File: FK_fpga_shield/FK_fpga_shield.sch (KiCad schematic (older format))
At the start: 3 parts

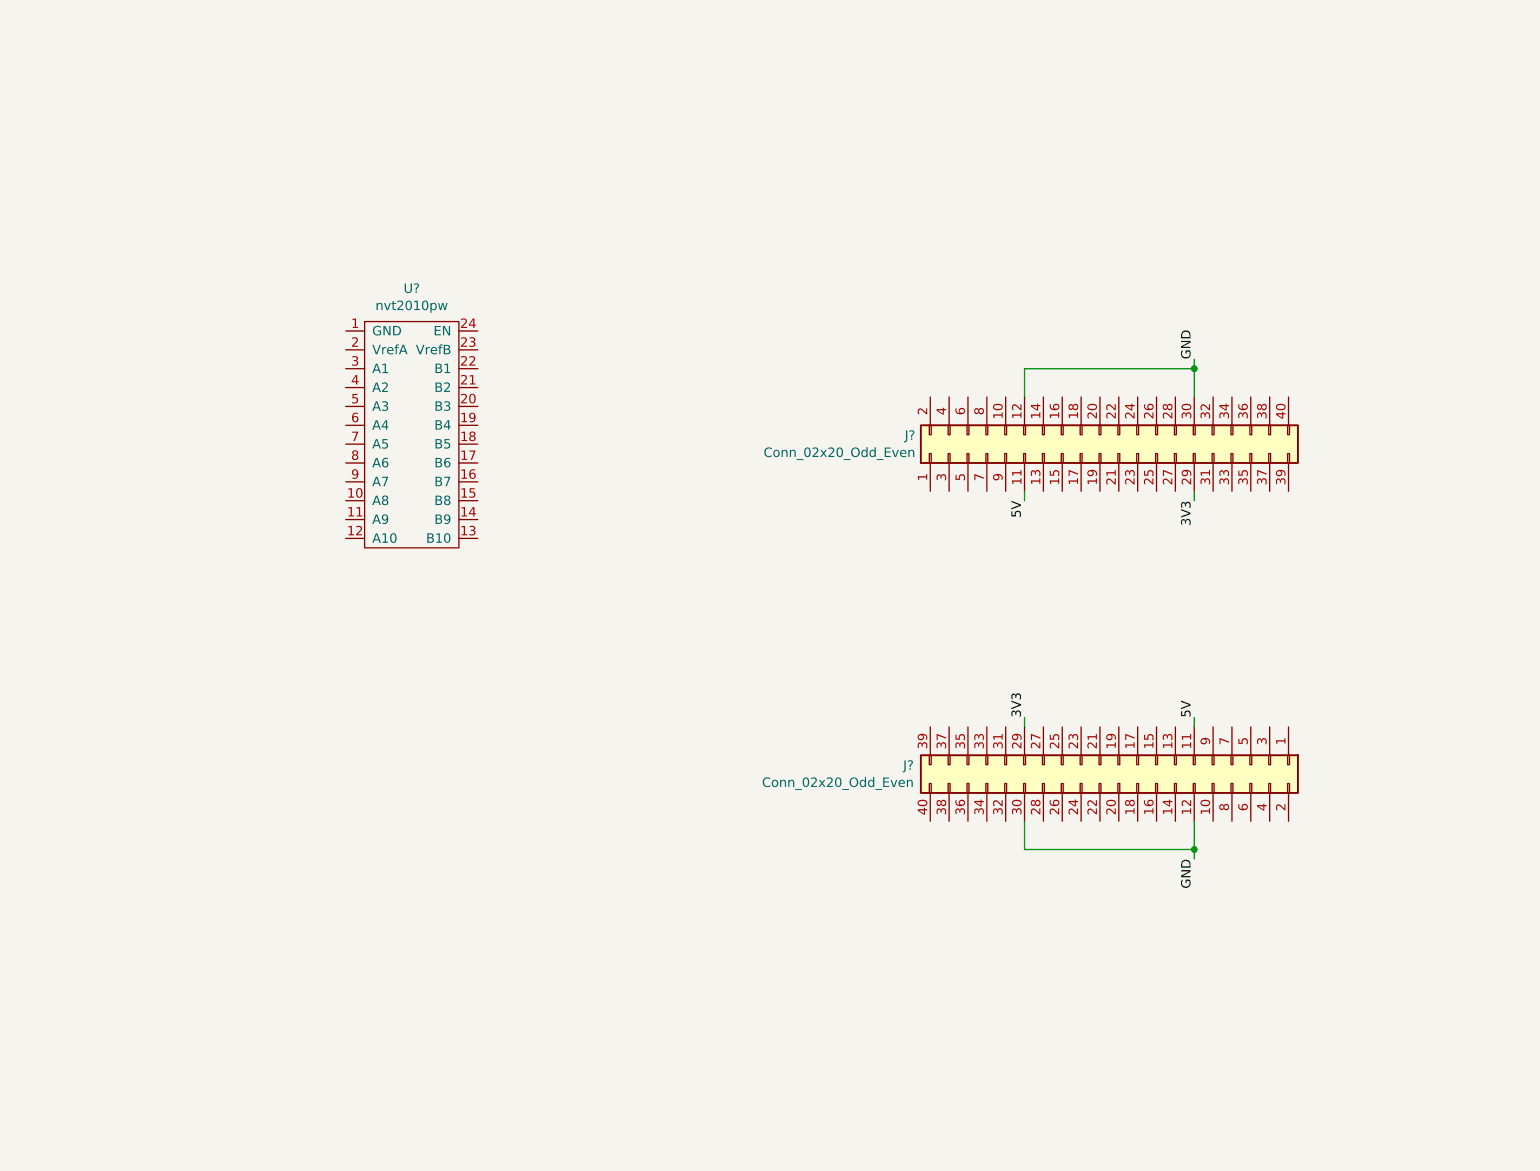
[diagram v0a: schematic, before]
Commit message: pre conn symbol rework
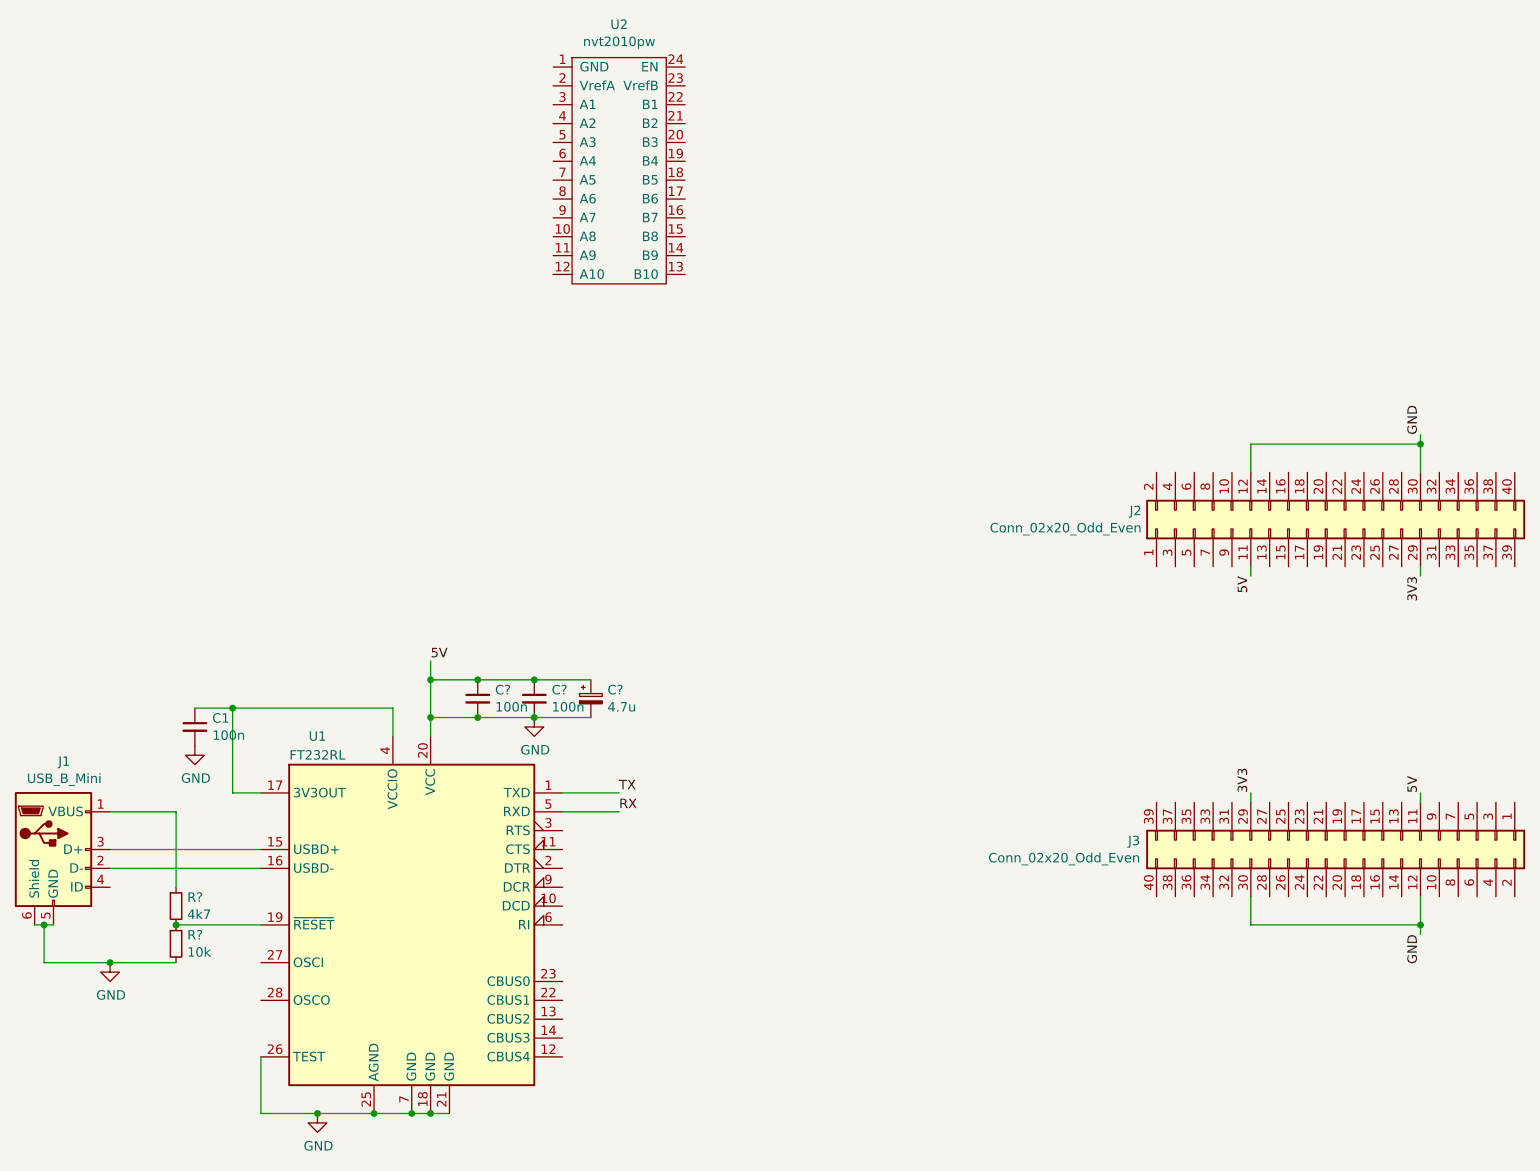
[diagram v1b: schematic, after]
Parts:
- added C1, C? (x2): 100n, symbol Device:C_Small
- added C?: 4.7u, symbol Device:CP_Small
- added J1: USB_B_Mini, 54819-0519:54819-0519, symbol Connector:USB_B_Mini
- added R?: 4k7, symbol Device:R_Small
- added R?: 10k, symbol Device:R_Small
- added U1: FT232RL, Package_SO:SSOP-28_5.3x10.2mm_P0.65mm, symbol Interface_USB:FT232RL
- gave numbers to parts that had none: 3
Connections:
- net 5V is gone; now on net GND: J2.11 (Pin_11), J3.11 (Pin_11)
- net GND: now also C1.2, C?.1, C?.1, C?.1, C?.2, C?.2, C?.2, J1.5 (GND), J1.6 (Shield), R?.2, U1.18 (GND), U1.20 (VCC), U1.21 (GND), U1.25 (AGND), U1.26 (TEST), U1.7 (GND)
- new net: J1.3 (D+), U1.15 (USBD+)
- new net: J1.2 (D-), U1.16 (USBD-)
- new net: C1.1, U1.17 (3V3OUT), U1.4 (VCCIO)
- new net: R?.1, R?.2, U1.19 (~RESET~)
- new net: J1.1 (VBUS), R?.1
- new net RX: U1.5 (RXD)
- new net TX: U1.1 (TXD)
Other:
- moved on the sheet: J2, J3, U2

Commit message: pre symbol update
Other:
- note added: "External oscillator not reqired\nper datasheet when 5V powered.\nTODO: consider adding footprint\njust in case"
- moved on the sheet: J2, J3, U2
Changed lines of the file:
@@
 L Connector_Generic:Conn_02x20_Odd_Even J2
 U 1 1 60371623
-P 7600 2850
-F 0 "J2" V 7696 3829 50  0000 L CNN
-F 1 "Conn_02x20_Odd_Even" V 7605 3829 50  0000 L CNN
-F 2 "Connector_PinSocket_2.54mm:PinSocket_2x20_P2.54mm_Vertical" H 7600 2850 50  0001 C CNN
-F 3 "~" H 7600 2850 50  0001 C CNN
-	1    7600 2850
+P 9400 2700
+F 0 "J2" V 9496 3679 50  0000 L CNN
+F 1 "Conn_02x20_Odd_Even" V 9405 3679 50  0000 L CNN
+F 2 "Connector_PinSocket_2.54mm:PinSocket_2x20_P2.54mm_Vertical" H 9400 2700 50  0001 C CNN
+F 3 "~" H 9400 2700 50  0001 C CNN
+	1    9400 2700
 	0    -1   -1   0
 $EndComp
@@
 L Connector_Generic:Conn_02x20_Odd_Even J3
 U 1 1 603774BB
-P 7700 4500
-F 0 "J3" V 7704 3413 50  0000 R CNN
-F 1 "Conn_02x20_Odd_Even" V 7795 3413 50  0000 R CNN
-F 2 "Connector_PinSocket_2.54mm:PinSocket_2x20_P2.54mm_Vertical" H 7700 4500 50  0001 C CNN
-F 3 "~" H 7700 4500 50  0001 C CNN
-	1    7700 4500
+P 9500 4350
+F 0 "J3" V 9504 3263 50  0000 R CNN
+F 1 "Conn_02x20_Odd_Even" V 9595 3263 50  0000 R CNN
+F 2 "Connector_PinSocket_2.54mm:PinSocket_2x20_P2.54mm_Vertical" H 9500 4350 50  0001 C CNN
+F 3 "~" H 9500 4350 50  0001 C CNN
+	1    9500 4350
 	0    1    1    0
 $EndComp
 Wire Wire Line
-	7200 4800 7200 4950
-Wire Wire Line
-	7200 4950 8100 4950
-Wire Wire Line
-	8100 4950 8100 4800
-Text Label 8100 5000 3    50   ~ 0
+	9000 4650 9000 4800
+Wire Wire Line
+	9000 4800 9900 4800
+Wire Wire Line
+	9900 4800 9900 4650
+Text Label 9900 4850 3    50   ~ 0
 GND
 Wire Wire Line
-	8100 4950 8100 5000
-Connection ~ 8100 4950
-Text Label 8100 4250 1    50   ~ 0
+	9900 4800 9900 4850
+Connection ~ 9900 4800
+Text Label 9900 4100 1    50   ~ 0
 5V
 Wire Wire Line
-	8100 4250 8100 4300
-Text Label 7200 4250 1    50   ~ 0
+	9900 4100 9900 4150
+Text Label 9000 4100 1    50   ~ 0
 3V3
 Wire Wire Line
-	7200 4250 7200 4300
-Text Label 8100 3100 3    50   ~ 0
+	9000 4100 9000 4150
+Text Label 9900 2950 3    50   ~ 0
 3V3
 Wire Wire Line
-	8100 3100 8100 3050
-Text Label 7200 3100 3    50   ~ 0
+	9900 2950 9900 2900
+Text Label 9000 2950 3    50   ~ 0
 5V
 Wire Wire Line
-	7200 3100 7200 3050
-Wire Wire Line
-	7200 2550 7200 2400
-Wire Wire Line
-	7200 2400 8100 2400
-Wire Wire Line
-	8100 2400 8100 2550
-Text Label 8100 2350 1    50   ~ 0
+	9000 2950 9000 2900
+Wire Wire Line
+	9000 2400 9000 2250
+Wire Wire Line
+	9000 2250 9900 2250
+Wire Wire Line
+	9900 2250 9900 2400
+Text Label 9900 2200 1    50   ~ 0
 GND
 Wire Wire Line
-	8100 2350 8100 2400
-Connection ~ 8100 2400
+	9900 2200 9900 2250
+Connection ~ 9900 2250
 $Comp
 L FK_fpga_shield_custom_symbols:nvt2010pw U2
 U 1 1 6038132A
-P 3850 950
-F 0 "U2" H 3850 1725 50  0000 C CNN
-F 1 "nvt2010pw" H 3850 1634 50  0000 C CNN
-F 2 "" V 3850 950 50  0001 C CNN
-F 3 "" V 3850 950 50  0001 C CNN
-	1    3850 950
+P 3100 1400
+F 0 "U2" H 3100 2175 50  0000 C CNN
+F 1 "nvt2010pw" H 3100 2084 50  0000 C CNN
+F 2 "" V 3100 1400 50  0001 C CNN
+F 3 "" V 3100 1400 50  0001 C CNN
+	1    3100 1400
 	1    0    0    -1
 $EndComp
@@
 	1    0    0    -1
 $EndComp
+Text Notes 600  5750 0    50   ~ 0
+External oscillator not reqired\nper datasheet when 5V powered.\nTODO: consider adding footprint\njust in case
 $EndSCHEMATC

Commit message: change connector sym/footprint on fpgashield
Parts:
- added J? (x3): molex-35363-0660, FK_fpga_shield_custom_footprints:molex-35363-0660, symbol FK_fpga_shield_custom_symbols:molex-35363-0660
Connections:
- net at U2.3 (A1): now also J?.3 (C_A)
- net at U2.4 (A2): now also J?.1 (C_B)
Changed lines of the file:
@@
 Text Notes 600  5750 0    50   ~ 0
 External oscillator not reqired\nper datasheet when 5V powered.\nTODO: consider adding footprint\njust in case
+$Comp
+L FK_fpga_shield_custom_symbols:molex-35363-0660 J?
+U 1 1 603AA77E
+P 2150 1100
+F 0 "J?" H 1650 1150 50  0000 C CNN
+F 1 "molex-35363-0660" H 1300 1050 50  0000 C CNN
+F 2 "FK_fpga_shield_custom_footprints:molex-35363-0660" H 2400 1100 50  0001 C CNN
+F 3 "" H 2400 1100 50  0001 C CNN
+	1    2150 1100
+	1    0    0    -1
+$EndComp
+Wire Wire Line
+	2450 1050 2750 1050
+Wire Wire Line
+	2750 1150 2450 1150
+$Comp
+L FK_fpga_shield_custom_symbols:molex-35363-0660 J?
+U 1 1 603AE109
+P 2150 1300
+F 0 "J?" H 1650 1350 50  0000 C CNN
+F 1 "molex-35363-0660" H 1300 1250 50  0000 C CNN
+F 2 "FK_fpga_shield_custom_footprints:molex-35363-0660" H 2400 1300 50  0001 C CNN
+F 3 "" H 2400 1300 50  0001 C CNN
+	1    2150 1300
+	1    0    0    -1
+$EndComp
+$Comp
+L FK_fpga_shield_custom_symbols:molex-35363-0660 J?
+U 1 1 603AE4E4
+P 2150 1500
+F 0 "J?" H 1650 1550 50  0000 C CNN
+F 1 "molex-35363-0660" H 1300 1450 50  0000 C CNN
+F 2 "FK_fpga_shield_custom_footprints:molex-35363-0660" H 2400 1500 50  0001 C CNN
+F 3 "" H 2400 1500 50  0001 C CNN
+	1    2150 1500
+	1    0    0    -1
+$EndComp
 $EndSCHEMATC

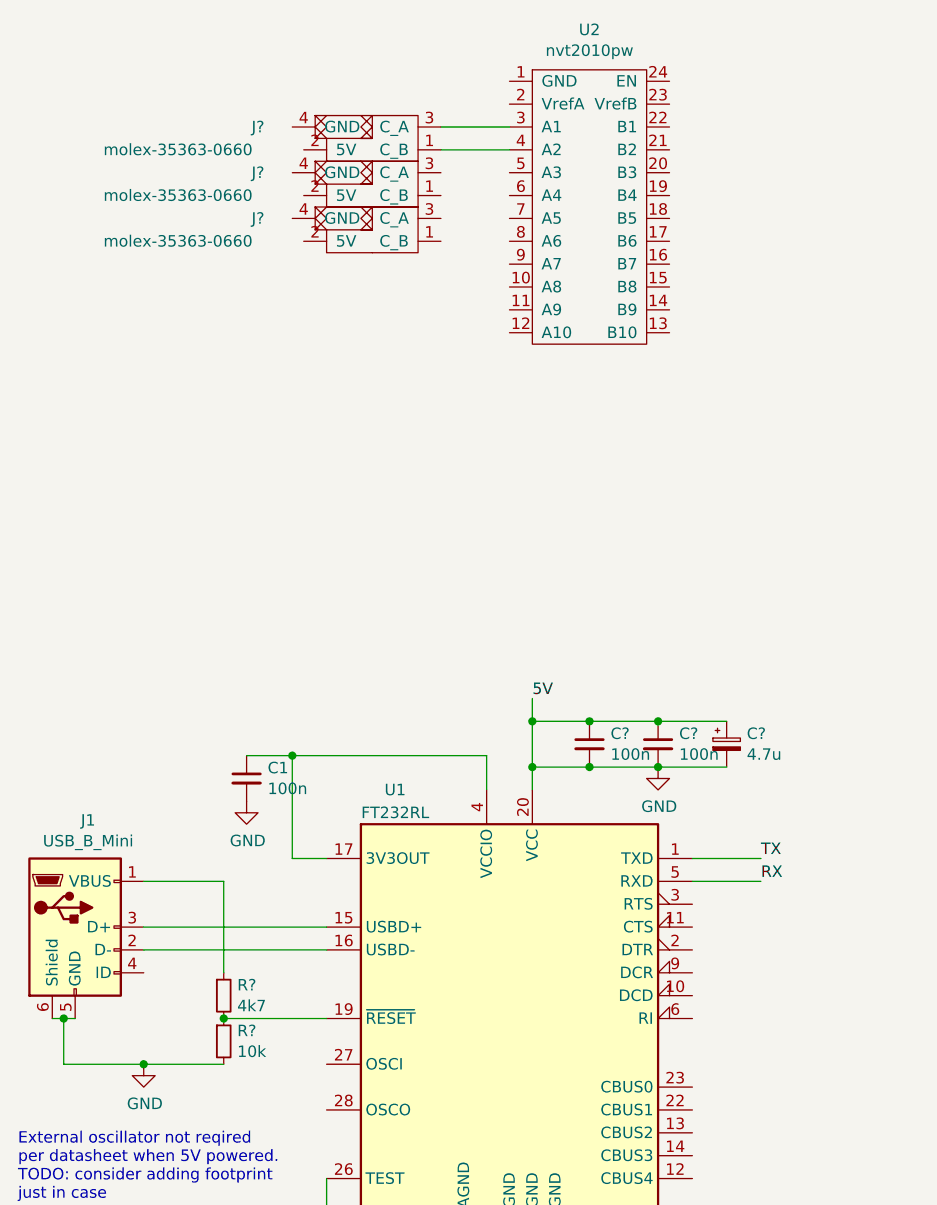
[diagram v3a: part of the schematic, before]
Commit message: change connector to microclasp 4 wire
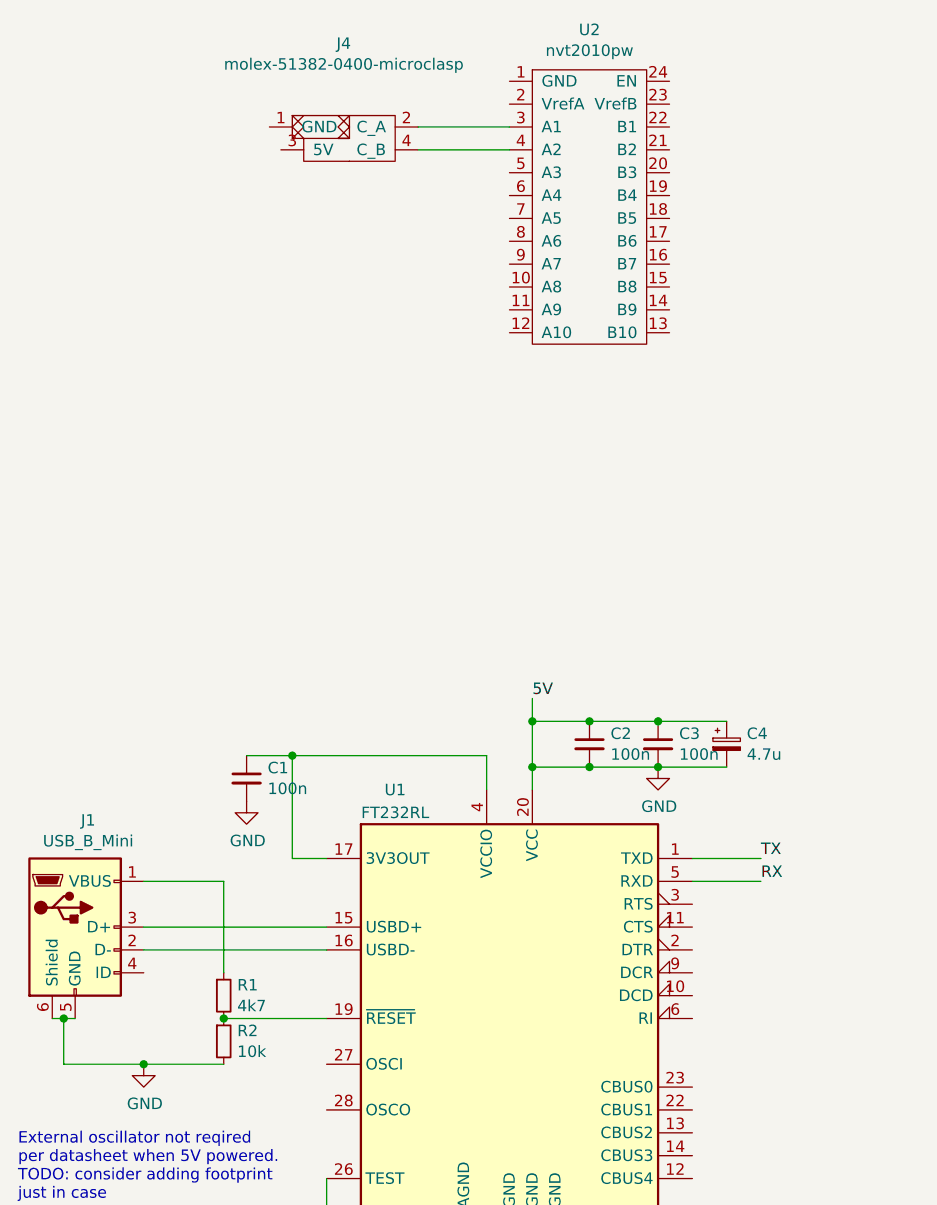
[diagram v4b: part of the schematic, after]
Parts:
- removed J? (x3): molex-35363-0660, FK_fpga_shield_custom_footprints:molex-35363-0660, symbol FK_fpga_shield_custom_symbols:molex-35363-0660
- added J4: molex-51382-0400-microclasp, FK_fpga_shield_custom_footprints:Molex_MicroClasp_55935-0410_1x04_P2.00mm_Horizontal_3DMODEL, symbol FK_fpga_shield_custom_symbols:molex-51382-0400-microclasp
- gave numbers to parts that had none: 5
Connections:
- net at U2.3 (A1): now also J4.2 (C_A)
- net at U2.4 (A2): now also J4.4 (C_B)
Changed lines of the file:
@@
 $EndComp
 $Comp
-L Device:R_Small R?
+L Device:R_Small R1
 U 1 1 603B5184
 P 1500 4850
-F 0 "R?" H 1559 4896 50  0000 L CNN
+F 0 "R1" H 1559 4896 50  0000 L CNN
 F 1 "4k7" H 1559 4805 50  0000 L CNN
 F 2 "" H 1500 4850 50  0001 C CNN
@@
 $EndComp
 $Comp
-L Device:R_Small R?
+L Device:R_Small R2
 U 1 1 603B60A2
 P 1500 5050
-F 0 "R?" H 1559 5096 50  0000 L CNN
+F 0 "R2" H 1559 5096 50  0000 L CNN
 F 1 "10k" H 1559 5005 50  0000 L CNN
 F 2 "" H 1500 5050 50  0001 C CNN
@@
 5V
 $Comp
-L Device:C_Small C?
+L Device:C_Small C2
 U 1 1 603B9C1A
 P 3100 3750
-F 0 "C?" H 3192 3796 50  0000 L CNN
+F 0 "C2" H 3192 3796 50  0000 L CNN
 F 1 "100n" H 3192 3705 50  0000 L CNN
 F 2 "" H 3100 3750 50  0001 C CNN
@@
 $EndComp
 $Comp
-L Device:C_Small C?
+L Device:C_Small C3
 U 1 1 603B9F93
 P 3400 3750
-F 0 "C?" H 3492 3796 50  0000 L CNN
+F 0 "C3" H 3492 3796 50  0000 L CNN
 F 1 "100n" H 3492 3705 50  0000 L CNN
 F 2 "" H 3400 3750 50  0001 C CNN
@@
 $EndComp
 $Comp
-L Device:CP_Small C?
+L Device:CP_Small C4
 U 1 1 603BB726
 P 3700 3750
-F 0 "C?" H 3788 3796 50  0000 L CNN
+F 0 "C4" H 3788 3796 50  0000 L CNN
 F 1 "4.7u" H 3788 3705 50  0000 L CNN
 F 2 "" H 3700 3750 50  0001 C CNN
@@
 	3400 3850 3700 3850
 $Comp
-L power:GND #PWR?
+L power:GND #PWR0104
 U 1 1 603BD551
 P 3400 3850
-F 0 "#PWR?" H 3400 3600 50  0001 C CNN
+F 0 "#PWR0104" H 3400 3600 50  0001 C CNN
 F 1 "GND" H 3405 3677 50  0000 C CNN
 F 2 "" H 3400 3850 50  0001 C CNN
@@
 External oscillator not reqired\nper datasheet when 5V powered.\nTODO: consider adding footprint\njust in case
 $Comp
-L FK_fpga_shield_custom_symbols:molex-35363-0660 J?
-U 1 1 603AA77E
-P 2150 1100
-F 0 "J?" H 1650 1150 50  0000 C CNN
-F 1 "molex-35363-0660" H 1300 1050 50  0000 C CNN
-F 2 "FK_fpga_shield_custom_footprints:molex-35363-0660" H 2400 1100 50  0001 C CNN
-F 3 "" H 2400 1100 50  0001 C CNN
-	1    2150 1100
+L FK_fpga_shield_custom_symbols:molex-51382-0400-microclasp J4
+U 1 1 603CD5AD
+P 2050 1100
+F 0 "J4" H 2025 1515 50  0000 C CNN
+F 1 "molex-51382-0400-microclasp" H 2025 1424 50  0000 C CNN
+F 2 "FK_fpga_shield_custom_footprints:Molex_MicroClasp_55935-0410_1x04_P2.00mm_Horizontal_3DMODEL" H 2300 1100 50  0001 C CNN
+F 3 "" H 2300 1100 50  0001 C CNN
+	1    2050 1100
 	1    0    0    -1
 $EndComp
 Wire Wire Line
-	2450 1050 2750 1050
+	2350 1050 2750 1050
 Wire Wire Line
-	2750 1150 2450 1150
-$Comp
-L FK_fpga_shield_custom_symbols:molex-35363-0660 J?
-U 1 1 603AE109
-P 2150 1300
-F 0 "J?" H 1650 1350 50  0000 C CNN
-F 1 "molex-35363-0660" H 1300 1250 50  0000 C CNN
-F 2 "FK_fpga_shield_custom_footprints:molex-35363-0660" H 2400 1300 50  0001 C CNN
-F 3 "" H 2400 1300 50  0001 C CNN
-	1    2150 1300
-	1    0    0    -1
-$EndComp
-$Comp
-L FK_fpga_shield_custom_symbols:molex-35363-0660 J?
-U 1 1 603AE4E4
-P 2150 1500
-F 0 "J?" H 1650 1550 50  0000 C CNN
-F 1 "molex-35363-0660" H 1300 1450 50  0000 C CNN
-F 2 "FK_fpga_shield_custom_footprints:molex-35363-0660" H 2400 1500 50  0001 C CNN
-F 3 "" H 2400 1500 50  0001 C CNN
-	1    2150 1500
-	1    0    0    -1
-$EndComp
+	2750 1150 2350 1150
 $EndSCHEMATC
